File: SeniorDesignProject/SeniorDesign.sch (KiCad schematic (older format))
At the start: 28 parts, among them J1 RJ45(LoadCells), J2 RJ45(Accelerometer), J3 PICkit3, J4 RJ11(ICD3), J5 ID-12LA Header, J6 XBEE Header, J7 7-Segment Display, P7 Power 1, P9 Power 2, U1 INA827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

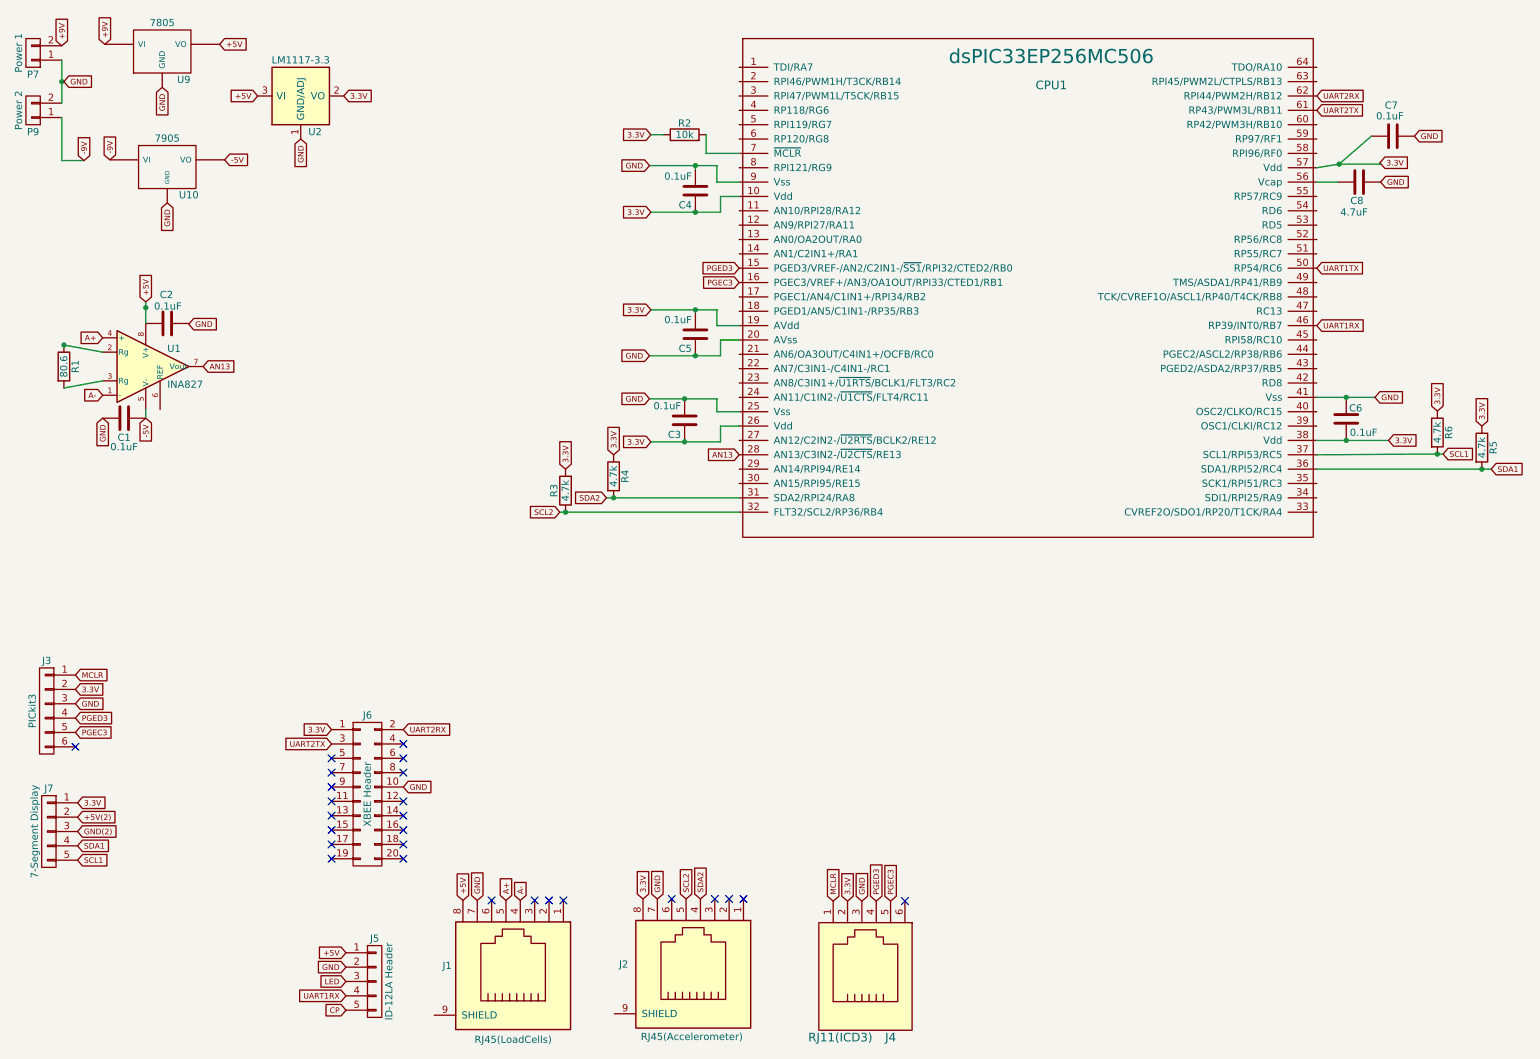
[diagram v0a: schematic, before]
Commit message: Added TL7660 +5V ro -5V converter, Removed 7905 Regulator Removed -9V connection
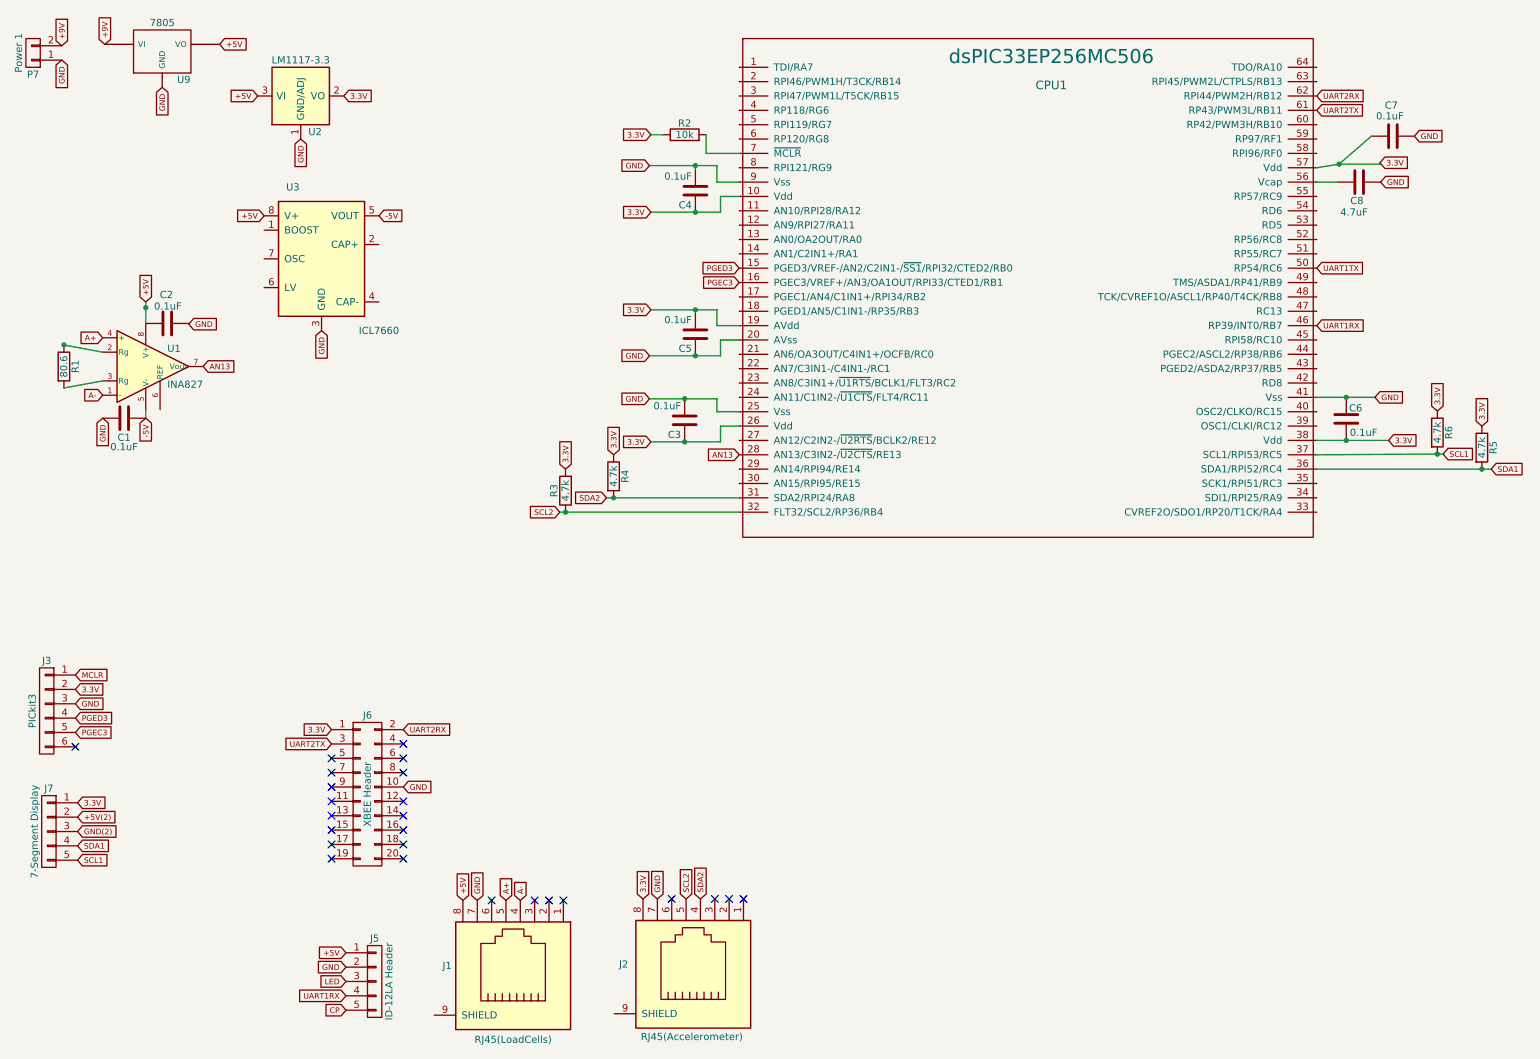
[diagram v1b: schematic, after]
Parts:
- removed J4: RJ11(ICD3), SeniorDesignFootprints:RJ11-6, symbol RJ11
- removed P9: Power 2, Pin_Headers:Pin_Header_Straight_1x02_Pitch3.96mm_Friction_Lock, symbol CONN_01X02
- removed U10: 7905, TO_SOT_Packages_THT:TO-92_Inline_Wide, symbol 7905
- added U3: ICL7660, Housings_DIP:DIP-8_W7.62mm, symbol ICL7660
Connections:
- net +5V: now also U3.8 (V+)
- net -5V: now also U3.5 (VOUT)
- net GND: now also U3.3 (GND)
- no-connect marks 26 -> 25
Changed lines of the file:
@@
-$EndComp
-$Comp
-L 7805 U9
-U 1 1 58461699
-P 1620 785
-F 0 "U9" H 1770 589 50  0000 C CNN
-F 1 "7805" H 1620 985 50  0000 C CNN
-F 2 "TO_SOT_Packages_THT:TO-92_Inline_Wide" H 1620 785 50  0001 C CNN
-F 3 "http://www.ti.com/lit/ds/symlink/lm7805.pdf" H 1620 785 50  0001 C CNN
-	1    1620 785
-	1    0    0    -1
-$EndComp
-$Comp
-L 7905 U10
-U 1 1 584617C8
-P 1655 1590
-F 0 "U10" H 1805 1395 50  0000 C CNN
-F 1 "7905" H 1655 1790 50  0000 C CNN
-F 2 "TO_SOT_Packages_THT:TO-92_Inline_Wide" H 1655 1590 50  0001 C CNN
-F 3 "http://www.ti.com/lit/ds/symlink/lm7905.pdf" H 1655 1590 50  0001 C CNN
-	1    1655 1590
-	1    0    0    -1
 $EndComp
 $Comp
@@
 $EndComp
 $Comp
-L CONN_01X02 P9
-U 1 1 58AD41C9
-P 720 1195
-F 0 "P9" H 720 1345 50  0000 C CNN
-F 1 "Power 2" V 820 1195 50  0000 C CNN
-F 2 "Pin_Headers:Pin_Header_Straight_1x02_Pitch3.96mm_Friction_Lock" H 720 1195 50  0001 C CNN
-F 3 "" H 720 1195 50  0000 C CNN
-	1    720  1195
-	-1   0    0    1
-$EndComp
-$Comp
 L CONN_02X10 J6
 U 1 1 58ACD0F4
@@
 	1    3050 5960
 	1    0    0    -1
-$EndComp
-$Comp
-L RJ11 J4
-U 1 1 58ACD97B
-P 6495 7155
-F 0 "J4" H 6695 7655 60  0000 C CNN
-F 1 "RJ11(ICD3)" H 6345 7655 60  0000 C CNN
-F 2 "SeniorDesignFootprints:RJ11-6" H 6495 7155 60  0001 C CNN
-F 3 "" H 6495 7155 60  0001 C CNN
-	1    6495 7155
-	1    0    0    1
 $EndComp
 $Comp
@@
 Text GLabel 5640 2395 0    39   Input ~ 0
 PGEC3
-Text GLabel 6295 6705 1    39   Input ~ 0
-MCLR
-Text GLabel 6395 6705 1    39   Input ~ 0
-3.3V
-Text GLabel 6495 6705 1    39   Input ~ 0
-GND
-Text GLabel 6595 6705 1    39   Input ~ 0
-PGED3
-Text GLabel 6695 6705 1    39   Input ~ 0
-PGEC3
-NoConn ~ 6795 6705
 Text GLabel 1015 5130 2    39   Input ~ 0
 MCLR
@@
 	1    0    0    -1
 $EndComp
-Text GLabel 1620 1035 3    39   Input ~ 0
-GND
-Text GLabel 2020 735  2    39   Input ~ 0
-+5V
 $Comp
 L LM1117-3.3 U2
@@
 	1    0    0    -1
 $EndComp
-Wire Wire Line
-	920  845  920  1145
-Text GLabel 935  995  2    39   Input ~ 0
-GND
-Wire Wire Line
-	935  995  920  995
-Connection ~ 920  995
-Wire Wire Line
-	920  1245 920  1545
-Wire Wire Line
-	920  1545 1075 1545
-Text GLabel 1655 1840 3    39   Input ~ 0
-GND
-Text GLabel 2055 1540 2    39   Input ~ 0
--5V
+Text GLabel 920  845  3    39   Input ~ 0
+GND
 Text GLabel 2285 1095 0    39   Input ~ 0
 +5V
@@
 Text GLabel 920  745  1    39   Input ~ 0
 +9V
+$Comp
+L ICL7660 U3
+U 1 1 58B9FDD5
+P 2730 2230
+F 0 "U3" H 2530 2730 50  0000 C CNN
+F 1 "ICL7660" H 3130 1730 50  0000 C CNN
+F 2 "Housings_DIP:DIP-8_W7.62mm" H 2830 2130 50  0001 C CNN
+F 3 "" H 2830 2130 50  0001 C CNN
+	1    2730 2230
+	1    0    0    -1
+$EndComp
+Text GLabel 2730 2730 3    39   Input ~ 0
+GND
+Text GLabel 2330 1930 0    39   Input ~ 0
++5V
+Text GLabel 3130 1930 2    39   Input ~ 0
+-5V
+Text GLabel 1620 1035 3    39   Input ~ 0
+GND
+Text GLabel 2020 735  2    39   Input ~ 0
++5V
 Text GLabel 1220 735  1    39   Input ~ 0
 +9V
-Text GLabel 1075 1545 1    39   Input ~ 0
--9V
-Text GLabel 1255 1540 1    39   Input ~ 0
--9V
+$Comp
+L 7805 U9
+U 1 1 58461699
+P 1620 785
+F 0 "U9" H 1770 589 50  0000 C CNN
+F 1 "7805" H 1620 985 50  0000 C CNN
+F 2 "TO_SOT_Packages_THT:TO-92_Inline_Wide" H 1620 785 50  0001 C CNN
+F 3 "http://www.ti.com/lit/ds/symlink/lm7805.pdf" H 1620 785 50  0001 C CNN
+	1    1620 785
+	1    0    0    -1
+$EndComp
 $EndSCHEMATC

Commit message: Added TC7660 +5V to -5V converter Removed -9V power Removed 7905 -9V to -5V regulator
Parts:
- U3: footprint Housings_DIP:DIP-8_W7.62mm -> Housings_SOIC:SOIC-8_3.9x4.9mm_Pitch1.27mm
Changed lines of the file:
@@
 F 0 "U3" H 2530 2730 50  0000 C CNN
 F 1 "ICL7660" H 3130 1730 50  0000 C CNN
-F 2 "Housings_DIP:DIP-8_W7.62mm" H 2830 2130 50  0001 C CNN
+F 2 "Housings_SOIC:SOIC-8_3.9x4.9mm_Pitch1.27mm" H 2830 2130 50  0001 C CNN
 F 3 "" H 2830 2130 50  0001 C CNN
 	1    2730 2230

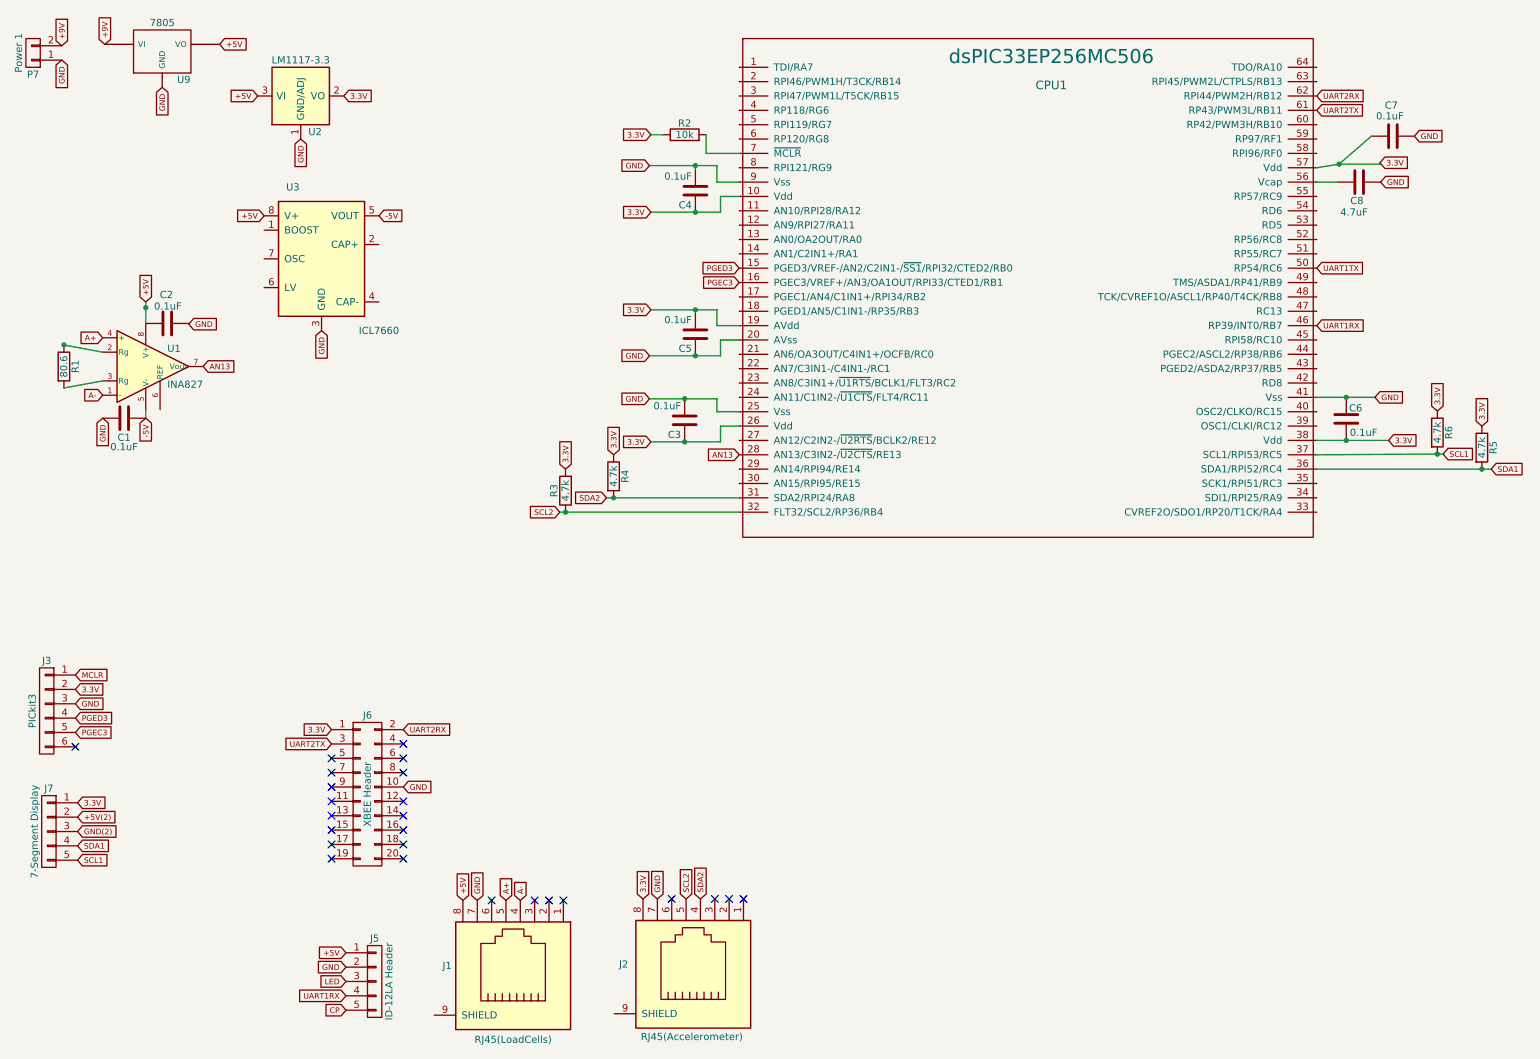
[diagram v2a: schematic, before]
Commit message: Changed accelerometer to SPI rather than I2C
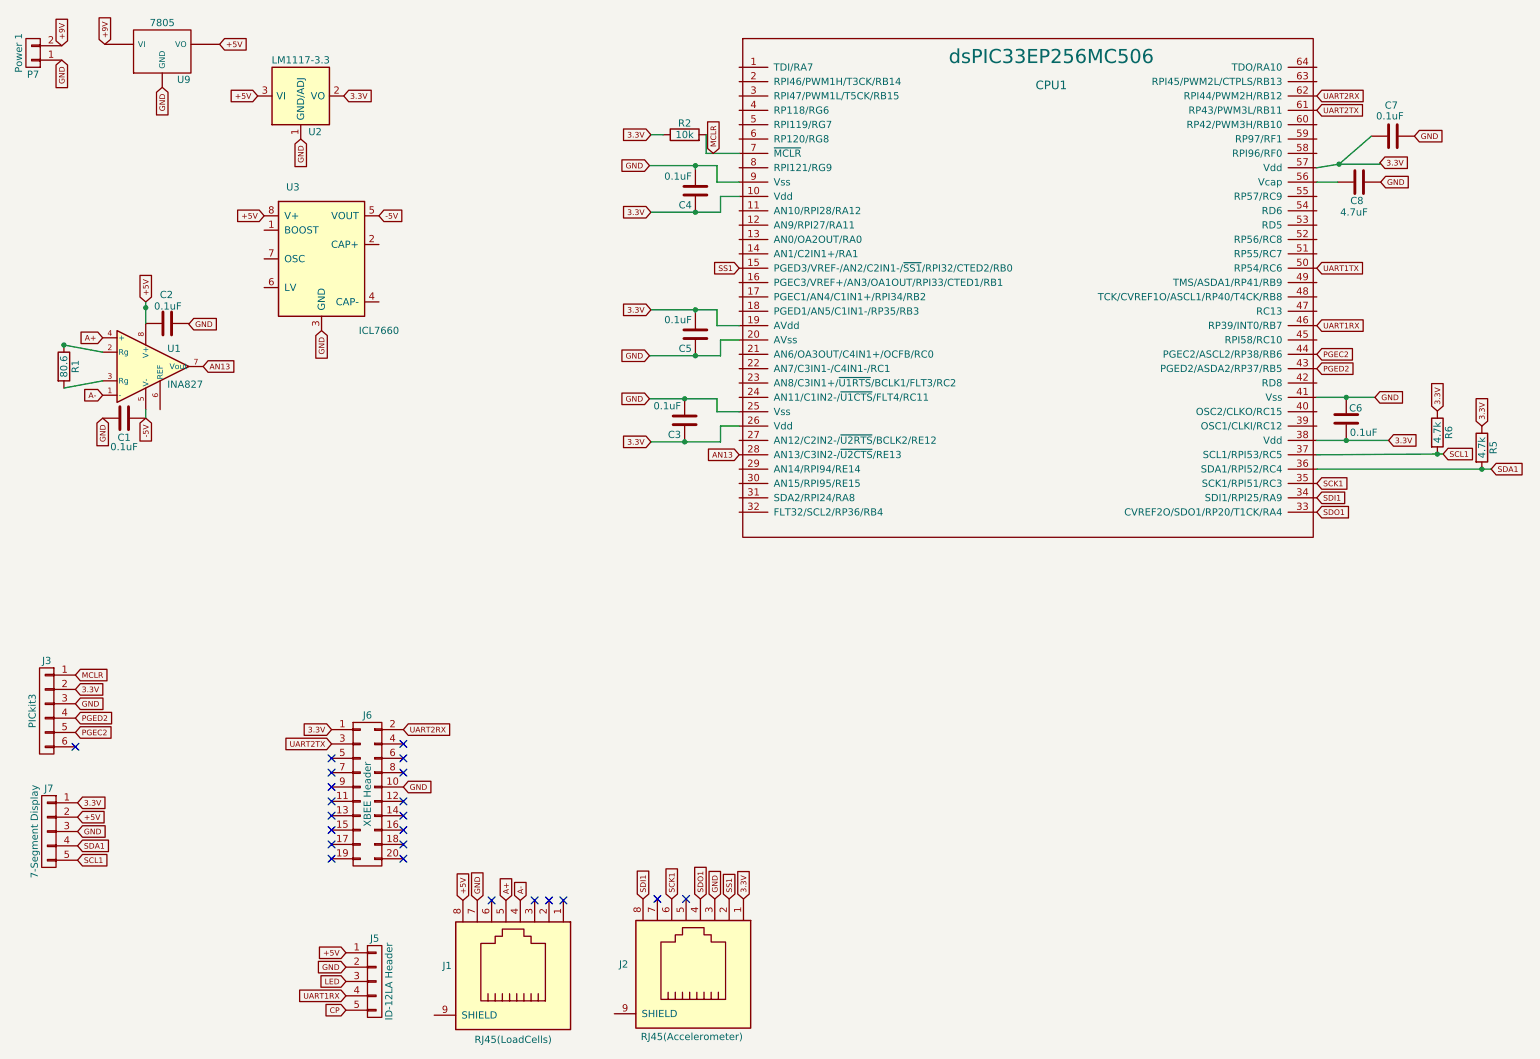
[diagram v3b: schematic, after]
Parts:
- removed R3, R4: 4.7k, Resistors_SMD:R_0805, symbol R
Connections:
- net +5V(2) is gone; now on net +5V: J7.2 (P2)
- net GND(2) is gone; now on net GND: J7.3 (P3)
- net 3.3V: now also J2.1; no longer J2.8
- net GND: now also J2.3; no longer J2.7
- net MCLR: now also CPU1.7 (~MCLR), R2.2
- net SDO1: now reaches CPU1.33 (CVREF2O/SDO1/RP20/T1CK/RA4)
- net SDO1: now also J2.4
- net SDI1: now reaches CPU1.34 (SDI1/RPI25/RA9)
- net SDI1: now also J2.8
- net SCK1: now reaches CPU1.35 (SCK1/RPI51/RC3)
- net SCK1: now also J2.6
- net PGED2: now reaches CPU1.43 (PGED2/ASDA2/RP37/RB5)
- net PGED2: now also J3.4 (P4)
- net PGEC2: now reaches CPU1.44 (PGEC2/ASCL2/RP38/RB6)
- net PGEC2: now also J3.5 (P5)
- net SS1: now reaches J2.2
- net SS1: now also CPU1.15 (PGED3/VREF-/AN2/C2IN1-/~SS1~/RPI32/CTED2/RB0)
- net PGEC3: no longer names the net of CPU1.16 (PGEC3/VREF+/AN3/OA1OUT/RPI33/CTED1/RB1)
- net PGEC3: no longer J3.5 (P5)
- removed net PGED3: CPU1.15 (PGED3/VREF-/AN2/C2IN1-/~SS1~/RPI32/CTED2/RB0), J3.4 (P4)
- net SCL2: no longer names the net of CPU1.32 (FLT32/SCL2/RP36/RB4)
- net SCL2: no longer J2.5
- net SDA2: no longer names the net of CPU1.31 (SDA2/RPI24/RA8)
- net SDA2: no longer J2.4
- no-connect marks 25 -> 23
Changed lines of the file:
@@
 Wire Wire Line
 	935  3130 1205 3080
-Text GLabel 4970 6690 1    39   Input ~ 0
-3.3V
-Text GLabel 5070 6690 1    39   Input ~ 0
-GND
-NoConn ~ 5170 6690
-Text GLabel 5270 6690 1    39   Input ~ 0
-SCL2
-Text GLabel 5370 6690 1    39   Input ~ 0
-SDA2
-NoConn ~ 5470 6690
-NoConn ~ 5570 6690
-NoConn ~ 5670 6690
-Text GLabel 4390 3995 0    39   Input ~ 0
-SCL2
-Text GLabel 4715 3895 0    39   Input ~ 0
-SDA2
-Text GLabel 5640 2295 0    39   Input ~ 0
-PGED3
-Text GLabel 5640 2395 0    39   Input ~ 0
-PGEC3
+Text GLabel 5470 6690 1    39   Input ~ 0
+GND
+Text GLabel 9665 2995 2    39   Input ~ 0
+PGED2
+Text GLabel 9665 2895 2    39   Input ~ 0
+PGEC2
 Text GLabel 1015 5130 2    39   Input ~ 0
 MCLR
@@
 GND
 Text GLabel 1015 5430 2    39   Input ~ 0
-PGED3
+PGED2
 Text GLabel 1015 5530 2    39   Input ~ 0
-PGEC3
+PGEC2
 NoConn ~ 1015 5630
 $Comp
@@
 3.3V
 Text GLabel 1030 6120 2    39   Input ~ 0
-+5V(2)
++5V
 Text GLabel 1030 6220 2    39   Input ~ 0
-GND(2)
+GND
 Text GLabel 1030 6320 2    39   Input ~ 0
 SDA1
@@
 3.3V
 Connection ~ 10505 3590
-Wire Wire Line
-	4715 3895 5640 3895
-$Comp
-L R R4
-U 1 1 58AEAF1C
-P 4765 3745
-F 0 "R4" V 4845 3745 50  0000 C CNN
-F 1 "4.7k" V 4765 3745 50  0000 C CNN
-F 2 "Resistors_SMD:R_0805" V 4695 3745 50  0001 C CNN
-F 3 "" H 4765 3745 50  0001 C CNN
-	1    4765 3745
-	1    0    0    -1
-$EndComp
-Text GLabel 4765 3595 1    39   Input ~ 0
-3.3V
-Connection ~ 4765 3895
-Wire Wire Line
-	4390 3995 5640 3995
-$Comp
-L R R3
-U 1 1 58AEB4D6
-P 4430 3845
-F 0 "R3" V 4510 3845 50  0000 C CNN
-F 1 "4.7k" V 4430 3845 50  0000 C CNN
-F 2 "Resistors_SMD:R_0805" V 4360 3845 50  0001 C CNN
-F 3 "" H 4430 3845 50  0001 C CNN
-	1    4430 3845
-	-1   0    0    1
-$EndComp
-Text GLabel 4430 3695 1    39   Input ~ 0
-3.3V
-Connection ~ 4430 3995
 Text GLabel 2800 5510 0    39   Input ~ 0
 3.3V
@@
 	1    0    0    -1
 $EndComp
+Text GLabel 5640 2295 0    39   Input ~ 0
+SS1
+Text GLabel 9665 3995 2    39   Input ~ 0
+SDO1
+Text GLabel 9665 3895 2    39   Input ~ 0
+SDI1
+Text GLabel 9665 3795 2    39   Input ~ 0
+SCK1
+Text GLabel 5670 6690 1    39   Input ~ 0
+3.3V
+Text GLabel 5570 6690 1    39   Input ~ 0
+SS1
+Text GLabel 5370 6690 1    39   Input ~ 0
+SDO1
+Text GLabel 5170 6690 1    39   Input ~ 0
+SCK1
+Text GLabel 4970 6690 1    39   Input ~ 0
+SDI1
+NoConn ~ 5070 6690
+NoConn ~ 5270 6690
+Text GLabel 5460 1495 1    39   Input ~ 0
+MCLR
 $EndSCHEMATC
